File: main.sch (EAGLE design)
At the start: 127 parts, among them Q1 2N2222, Q2 2N2222, Q3 2N2222, Q4 N_MOSFET_DEVSOT23-6L_PKG, U1 MAX_485_DEV3D, U2 BQ24072TRGTR_DEVBQ24072TRGTR, U3 LD1117S33CTR_DEVLD1117S33CTR, U4 ESP_32_WROVER_I_PKG, U5 USB_TO_UART_DEV, U6 AP9214L_DEV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

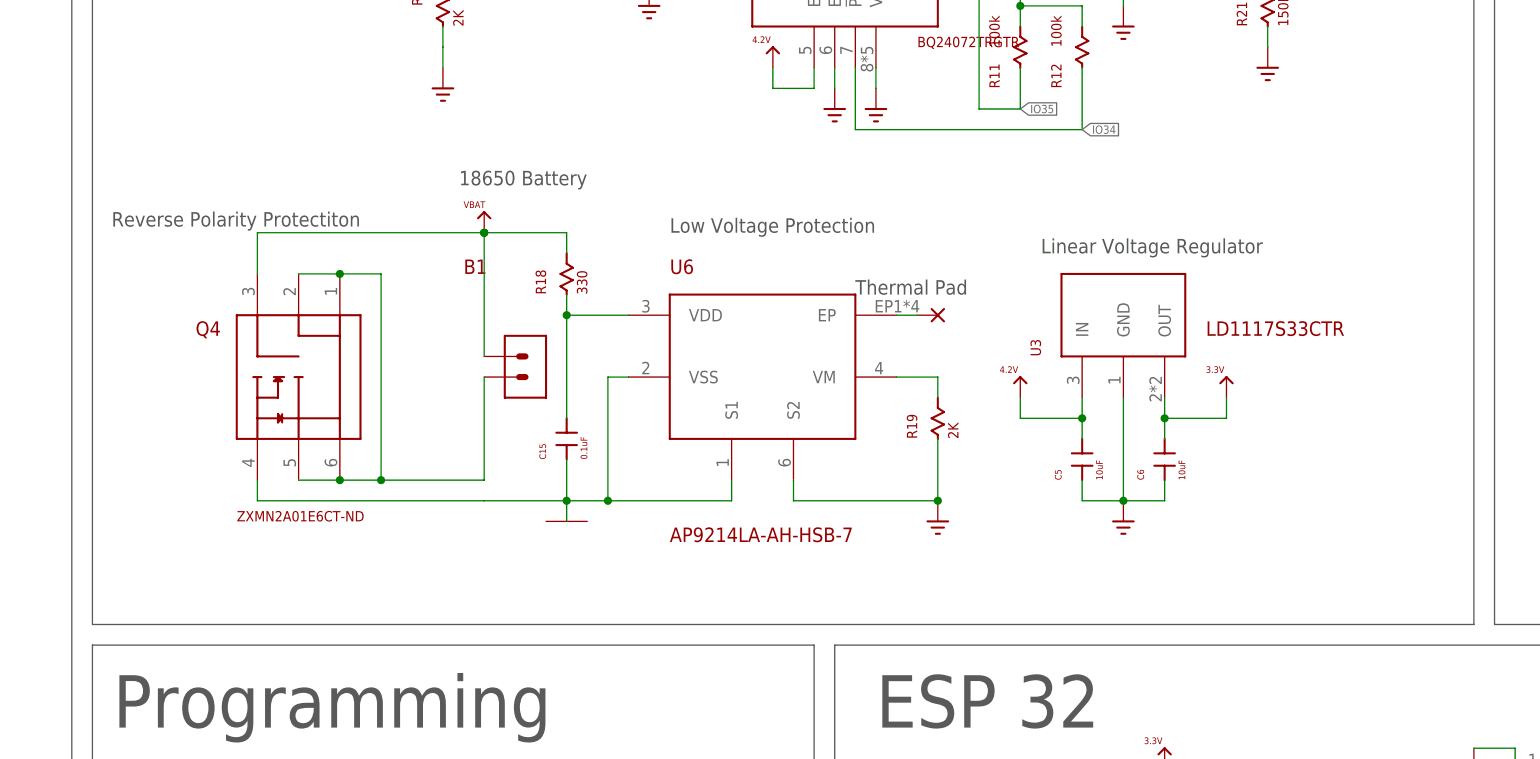
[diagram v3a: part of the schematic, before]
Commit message: redacted battery saftey chips
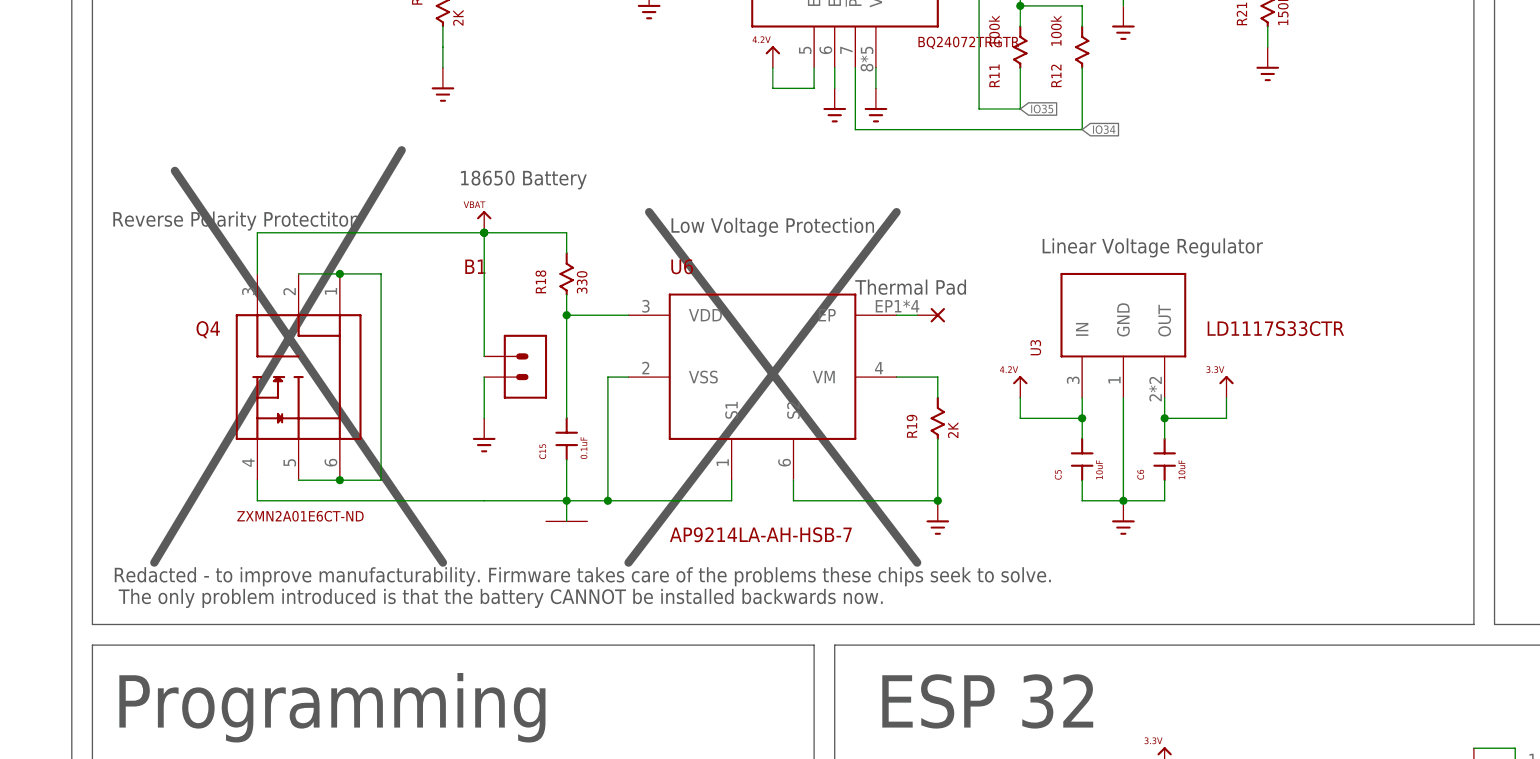
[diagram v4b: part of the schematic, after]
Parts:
- added GND21: GND, Blizzard_Library:GND
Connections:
- net BATTERY_GROUND: no longer B1.P$2
- net GND: now also B1.P$2, GND21.P$1
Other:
- note added: "Redacted - to improve manufacturability. Firmware takes care of the problems these chips seek to solve. The only problem introduced is that the battery CANNOT be installed backwards now."
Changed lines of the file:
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@@
 <?xml version="1.0" encoding="utf-8"?>
 <!DOCTYPE eagle SYSTEM "eagle.dtd">
-<eagle version="9.5.2">
+<eagle version="9.6.1">
 <drawing>
 <settings>
@@
 <part name="NC39" library="Blizzard_Library" library_urn="urn:adsk.eagle:library:2665040" deviceset="NC" device=""/>
 <part name="NC40" library="Blizzard_Library" library_urn="urn:adsk.eagle:library:2665040" deviceset="NC" device=""/>
-<part name="U2" library="Blizzard_Library" library_urn="urn:adsk.eagle:library:2665040" deviceset="BQ24072TRGTR_DEV" device="BQ24072TRGTR" package3d_urn="urn:adsk.eagle:package:7249956/11"/>
+<part name="U2" library="Blizzard_Library" library_urn="urn:adsk.eagle:library:2665040" deviceset="BQ24072TRGTR_DEV" device="BQ24072TRGTR" package3d_urn="urn:adsk.eagle:package:7249956/12"/>
+<part name="GND21" library="Blizzard_Library" library_urn="urn:adsk.eagle:library:2665040" deviceset="GND" device=""/>
 </parts>
 <sheets>
@@
 <text x="35.56" y="-152.4" size="1.778" layer="97" rot="R180">Reverse Polarity Protectiton</text>
 <text x="15.24" y="-167.64" size="1.778" layer="94">Q4</text>
+<wire x1="12.7" y1="-147.32" x2="45.72" y2="-195.58" width="1.016" layer="97"/>
+<wire x1="10.16" y1="-195.58" x2="40.64" y2="-144.78" width="1.016" layer="97"/>
+<wire x1="68.58" y1="-195.58" x2="101.6" y2="-152.4" width="1.016" layer="97"/>
+<wire x1="71.12" y1="-152.4" x2="104.14" y2="-195.58" width="1.016" layer="97"/>
+<text x="5.08" y="-200.66" size="1.778" layer="97">Redacted - to improve manufacturability. Firmware takes care of the problems these chips seek to solve.
+ The only problem introduced is that the battery CANNOT be installed backwards now.</text>
 </plain>
 <instances>
@@
 <attribute name="PN" x="104.14" y="-132.08" size="1.27" layer="94"/>
 </instance>
+<instance part="GND21" gate="G$1" x="50.8" y="-180.34" smashed="yes"/>
 </instances>
 <busses>
@@
 <wire x1="167.64" y1="-256.54" x2="167.64" y2="-261.62" width="0.1524" layer="91"/>
 </segment>
+<segment>
+<pinref part="B1" gate="G$1" pin="P$2"/>
+<wire x1="50.8" y1="-172.72" x2="50.8" y2="-177.8" width="0.1524" layer="91"/>
+<pinref part="GND21" gate="G$1" pin="P$1"/>
+</segment>
 </net>
 <net name="RXD0" class="0">
@@
 <wire x1="27.94" y1="-160.02" x2="33.02" y2="-160.02" width="0.1524" layer="91"/>
 <pinref part="Q4" gate="G$1" pin="D4"/>
-<pinref part="B1" gate="G$1" pin="P$2"/>
 <wire x1="33.02" y1="-185.42" x2="38.1" y2="-185.42" width="0.1524" layer="91"/>
-<wire x1="38.1" y1="-185.42" x2="50.8" y2="-185.42" width="0.1524" layer="91"/>
-<wire x1="50.8" y1="-185.42" x2="50.8" y2="-172.72" width="0.1524" layer="91"/>
 <pinref part="Q4" gate="G$1" pin="D3"/>
 <wire x1="27.94" y1="-185.42" x2="33.02" y2="-185.42" width="0.1524" layer="91"/>
@@
 <wire x1="38.1" y1="-160.02" x2="38.1" y2="-185.42" width="0.1524" layer="91"/>
 <junction x="33.02" y="-160.02"/>
-<junction x="38.1" y="-185.42"/>
 </segment>
 </net>
@@
 </drawing>
 <compatibility>
+<note version="6.3" minversion="6.2.2" severity="warning">
+Since Version 6.2.2 text objects can contain more than one line,
+which will not be processed correctly with this version.
+</note>
 <note version="8.2" severity="warning">
 Since Version 8.2, EAGLE supports online libraries. The ids
